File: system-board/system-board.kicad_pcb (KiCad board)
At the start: 2 copper layers, 23.9 x 79.6 mm, 15 parts, among them J1 Micro_SD_Card_Det2, J2 Conn_01x02_Socket, J3 Conn_01x02_Socket, J4 BTN_SOCKET, J5 QWIIC, Q1 IRLB8721, U1 MAX98357AETE+T

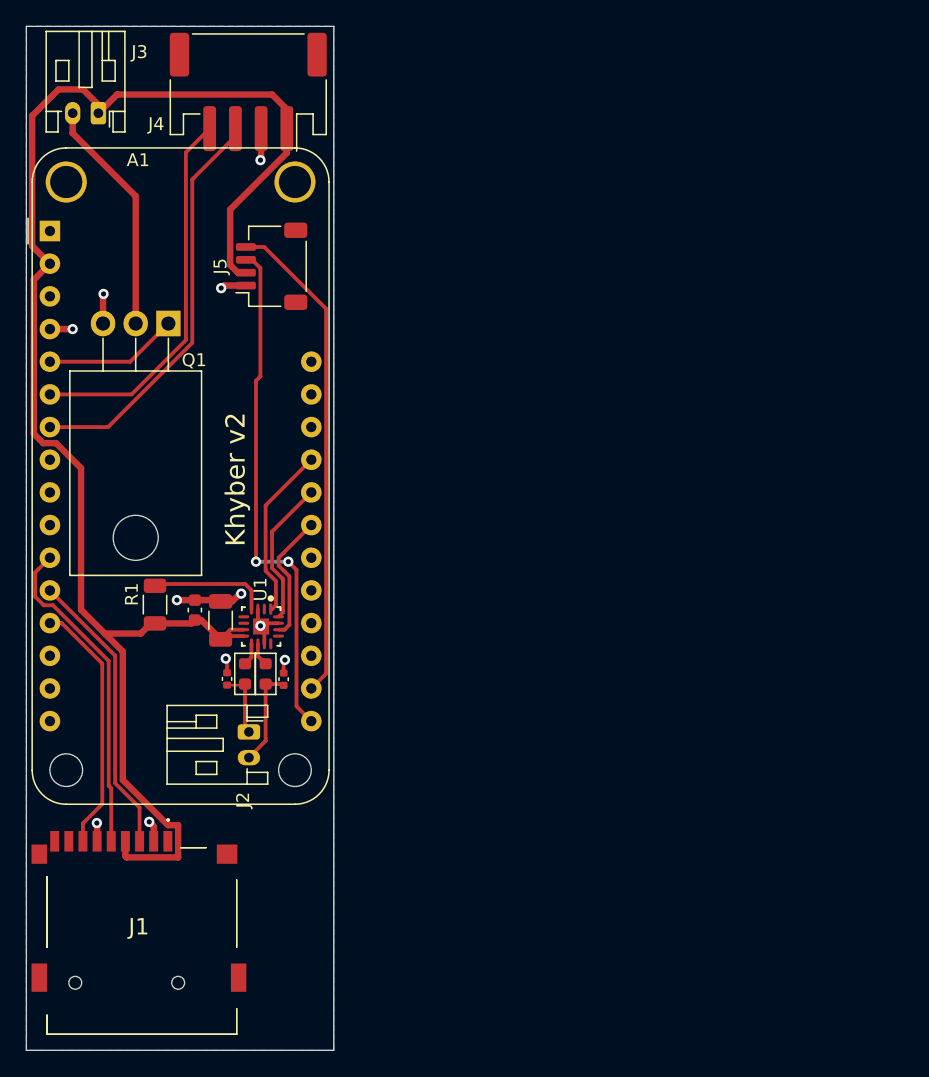
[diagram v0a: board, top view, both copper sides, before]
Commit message: Do some calculations, overhaul system-board to be a single board, not a Feather add-on.
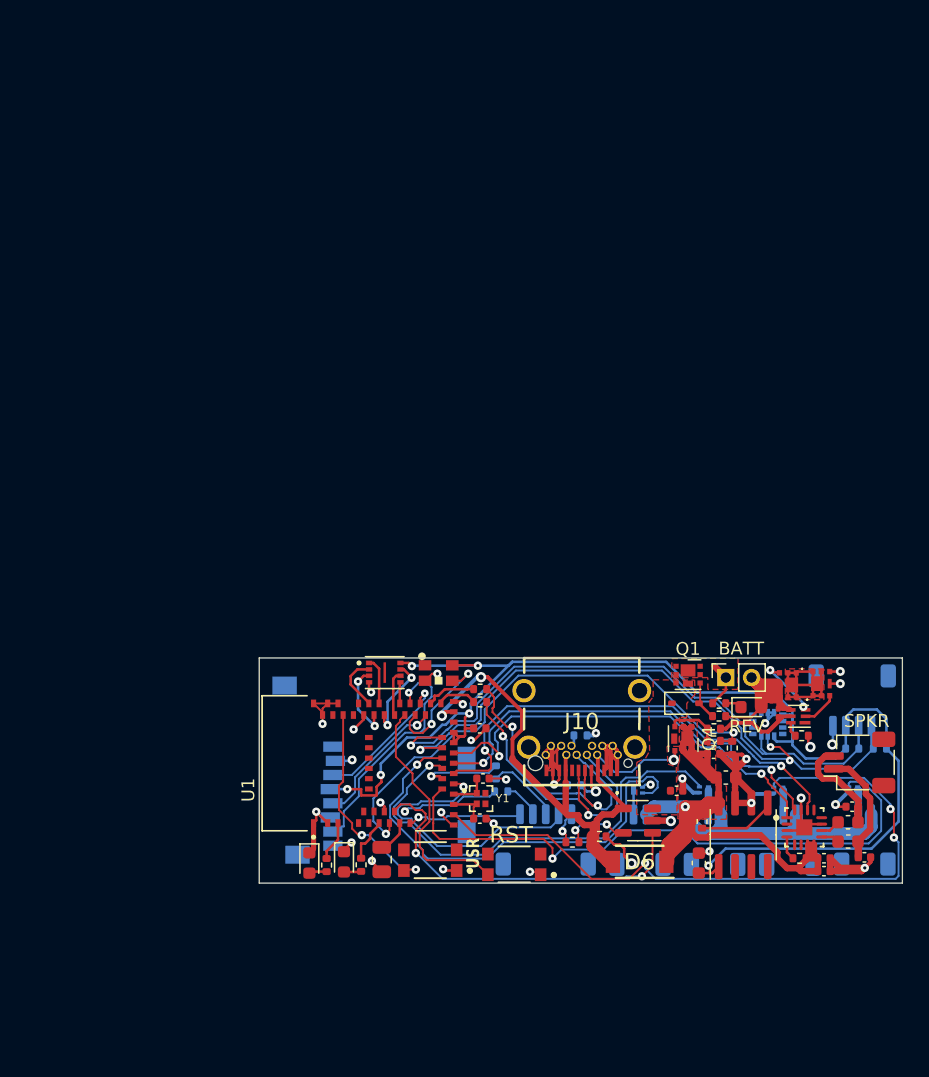
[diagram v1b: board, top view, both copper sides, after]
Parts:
- removed A1: Adafruit_Feather_Generic, Module:Adafruit_Feather_WithMountingHoles
- added C10: 0.1 uF, Capacitor_SMD:C_0201_0603Metric, F.Cu at (110.8, 95.4)
- added C11: 4.7u, Capacitor_SMD:C_0603_1608Metric, F.Cu at (106.7, 100.4)
- added C12: 4.7u, Capacitor_SMD:C_0603_1608Metric, F.Cu at (104.6, 107.0)
- added C15: 10u, Capacitor_SMD:C_0402_1005Metric, F.Cu at (105.7, 98.5)
- added C5: 220p, Capacitor_SMD:C_0402_1005Metric, F.Cu at (116.5, 102.7)
- added C6: 220p, Capacitor_SMD:C_0402_1005Metric, F.Cu at (117.5, 106.6)
- added C7: 10u, Capacitor_SMD:C_0402_1005Metric, F.Cu at (114.3, 106.7)
- added C8: 100 nF, Capacitor_SMD:C_0402_1005Metric, F.Cu at (114.3, 107.7)
- added C9: 10u, Capacitor_SMD:C_0402_1005Metric, F.Cu at (102.8, 101.4)
- added D1: WS2812B, Imports:WS2812B-2020, F.Cu at (84.3, 92.3)
- added D2: BLUE, LED_SMD:LED_0603_1608Metric, F.Cu at (74.3, 107.0)
- added D3: RED, LED_SMD:LED_0603_1608Metric, F.Cu at (77.0, 106.9)
- added D4: BZX38450, Diode_SMD:D_SOD-323, F.Cu at (103.5, 94.6)
- added D5: REV, LED_SMD:LED_0603_1608Metric, F.Cu at (108.6, 94.9)
- added D6: RSX501LAM20TR, Imports:SODFL4725X105N, F.Cu at (100.0, 106.9)
- added IC1: Flash_16Mb, Imports:USON-8-03x02mm-PSON50P200X300X50-9N, F.Cu at (80.2, 92.2)
- added IC2: LSM6DSLTR, Imports:LSM6DSLTR, B.Cu at (109.9, 96.3)
- added IC3: AP2115M-3.3TRG1, Package_SO:SOIC-8_3.9x4.9mm_P1.27mm, F.Cu at (108.0, 104.8)
- added J10: 217183-0001, Imports:Molex USB-C Horizontal 2171830001, F.Cu at (95.5, 96.0)
- added J6: BLADE_2, Connector_JST:JST_SH_SM02B-SRSS-TB_1x02-1MP_P1.00mm_Horizontal, B.Cu at (111.7, 105.3)
- added J7: BLADE_3, Connector_JST:JST_SH_SM02B-SRSS-TB_1x02-1MP_P1.00mm_Horizontal, B.Cu at (105.8, 105.3)
- added J8: BLADE_4, Connector_JST:JST_SH_SM02B-SRSS-TB_1x02-1MP_P1.00mm_Horizontal, B.Cu at (100.0, 105.3)
- added J9: BTNS, Connector_JST:JST_SH_SM05B-SRSS-TB_1x05-1MP_P1.00mm_Horizontal, B.Cu at (92.7, 105.2)
- added Q2: SSM6K504NU.LF, Imports:SSM6K504NULF, F.Cu at (114.1, 93.1)
- added Q3: SSM6K504NU.LF, Imports:SSM6K504NULF, F.Cu at (111.5, 93.2)
- added Q4: DMP1012UFDF, Imports:DMP1012UFDF, F.Cu at (103.4, 97.4)
- added Q5: PMZB290UNE2YL, Package_DFN_QFN:Diodes_DFN1006-3, B.Cu at (116.6, 101.3)
- added Q6: PMZB290UNE2YL, Package_DFN_QFN:Diodes_DFN1006-3, B.Cu at (110.8, 101.4)
- added Q7: PMZB290UNE2YL, Package_DFN_QFN:Diodes_DFN1006-3, B.Cu at (105.0, 101.3)
- added Q8: PMZB290UNE2YL, Package_DFN_QFN:Diodes_DFN1006-3, B.Cu at (99.8, 101.4)
- added R10: 1k, Resistor_SMD:R_0402_1005Metric, F.Cu at (106.2, 94.6)
- added R11: 2.0k, Resistor_SMD:R_0402_1005Metric, F.Cu at (94.8, 105.4)
- added R12: 200, Resistor_SMD:R_0402_1005Metric, F.Cu at (106.2, 95.6)
- added R13: 100k, Resistor_SMD:R_0402_1005Metric, F.Cu at (105.7, 97.5)
- added R14: 100k, Resistor_SMD:R_0402_1005Metric, F.Cu at (107.2, 98.1)
- added R15: 100k, Resistor_SMD:R_0402_1005Metric, F.Cu at (104.8, 103.8)
- added R16: 100k, Resistor_SMD:R_0402_1005Metric, F.Cu at (96.8, 105.0)
- added R2: 22, Resistor_SMD:R_0402_1005Metric, F.Cu at (87.6, 93.5)
- added R21: 1k, Resistor_SMD:R_0402_1005Metric, B.Cu at (88.8, 100.0)
- added R22: 1k, Resistor_SMD:R_0402_1005Metric, B.Cu at (89.2, 101.5)
- added R23: 5k1, Resistor_SMD:R_0402_1005Metric, B.Cu at (95.4, 97.1)
- added R24: 5k1, Resistor_SMD:R_0402_1005Metric, B.Cu at (94.9, 101.0)
- added R3: 1k, Resistor_SMD:R_0402_1005Metric, F.Cu at (75.6, 107.2)
- added R4: 1k, Resistor_SMD:R_0402_1005Metric, F.Cu at (78.3, 107.2)
- added R5: 2.0k, Resistor_SMD:R_0402_1005Metric, B.Cu at (116.5, 98.1)
- added R6: 2.0k, Resistor_SMD:R_0402_1005Metric, B.Cu at (118.7, 98.1)
- added R7: 1M, Resistor_SMD:R_0402_1005Metric, F.Cu at (112.4, 106.7)
- added R8: 330, Resistor_SMD:R_0402_1005Metric, F.Cu at (105.8, 96.6)
- added R9: 2.2k, Resistor_SMD:R_0402_1005Metric, F.Cu at (112.6, 97.1)
- added SW1: RST, Imports:CK_Components-KMR231NG_LFS-MFG, F.Cu at (90.2, 107.1)
- added SW2: USR, Imports:CK_Components-KMR231NG_LFS-MFG, F.Cu at (83.7, 106.8)
- added U2: MAX98357AETE+T, MaximCustom:Maxim_Integrated-T1633-4-0-V-IPC_C, F.Cu at (112.8, 104.3)
- added U3: BQ29705DSER, Package_SON:WSON-6_1.5x1.5mm_P0.5mm, F.Cu at (112.3, 95.6)
- added U4: MCP73832-2-OT, Package_TO_SOT_SMD:SOT-23-5, F.Cu at (99.8, 103.7)
- added Y1: 32.768k, Imports:XTAL_ECS-.327-12.5-1210B-N-TR, F.Cu at (87.7, 102.0)
- C1: footprint Capacitor_SMD:C_1206_3216Metric -> Capacitor_SMD:C_0402_1005Metric
- C2: value 0.1u -> 22p; footprint Capacitor_SMD:C_0603_1608Metric -> Capacitor_SMD:C_0402_1005Metric
- C3: value 220p -> 22p
- C4: value 220p -> 0.1 uF; footprint Capacitor_SMD:C_0402_1005Metric -> Capacitor_SMD:C_0805_2012Metric
- FB1, FB2: value FerriteBead_Small -> FB_Sm; footprint PCM_Ferrite_SMD_AKL:Ferrite_0603_1608Metric -> Capacitor_SMD:C_0603_1608Metric
- J1: value Micro_SD_Card_Det2 -> BATT; footprint TF-115:TF115 -> Connector_PinSocket_2.00mm:PinSocket_1x02_P2.00mm_Vertical
- J2: value Conn_01x02_Socket -> GTFP08431BEU; footprint Connector_JST:JST_PH_S2B-PH-K_1x02_P2.00mm_Horizontal -> Imports:GTFP08431BEU; moved to B.Cu
- J3: value Conn_01x02_Socket -> QWIIC; footprint Connector_JST:JST_PH_S2B-PH-K_1x02_P2.00mm_Horizontal -> Connector_JST:JST_SH_SM04B-SRSS-TB_1x04-1MP_P1.00mm_Horizontal; moved to B.Cu
- J4: value BTN_SOCKET -> SPKR; footprint Connector_JST:JST_PH_S4B-PH-SM4-TB_1x04-1MP_P2.00mm_Horizontal -> Connector_JST:JST_SH_SM02B-SRSS-TB_1x02-1MP_P1.00mm_Horizontal
- J5: value QWIIC -> BLADE_1; footprint Connector_JST:JST_SH_SM04B-SRSS-TB_1x04-1MP_P1.00mm_Horizontal -> Connector_JST:JST_SH_SM02B-SRSS-TB_1x02-1MP_P1.00mm_Horizontal; moved to B.Cu
- Q1: value IRLB8721 -> DMP1012UFDF; footprint Package_TO_SOT_THT:TO-220-3_Horizontal_TabDown -> Imports:DMP1012UFDF
- R1: value 1M -> 22; footprint Resistor_SMD:R_1206_3216Metric -> Resistor_SMD:R_0402_1005Metric
- U1: value MAX98357AETE+T -> MDBT50Q-1MV2; footprint MaximCustom:Maxim_Integrated-T1633-4-0-V-IPC_C -> Imports:XCVR_MDBT50Q-1MV2
- moved J3 74.3 mm to (116.5, 94.4), turned to 0 degrees
- moved J4 70.5 mm to (117.1, 99.2), turned to 90 degrees
- moved J5 64.1 mm to (117.5, 105.2), turned to 180 degrees
- moved J1 49.6 mm to (106.7, 92.6), turned to 90 degrees
- moved Q1 48.8 mm to (103.7, 92.4), turned to 0 degrees
- moved FB2 48.7 mm to (116.2, 105.4), turned to 180 degrees
- moved FB1 46.7 mm to (116.2, 103.9), turned to 180 degrees
- moved C2 27.4 mm to (87.5, 103.6), turned to 0 degrees
- moved R1 26.4 mm to (87.6, 94.5), turned to 180 degrees
- moved C1 21.8 mm to (87.5, 96.6), turned to 180 degrees
- moved C3 21.3 mm to (87.8, 100.5), turned to 0 degrees
- moved C4 16.0 mm to (79.9, 106.8), turned to 90 degrees
- moved U1 13.2 mm to (78.4, 99.3), turned to 90 degrees
- moved J2 10.3 mm to (79.5, 99.8), turned to 90 degrees
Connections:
- C2 pad 1: VCC -> /XL1
- C3 pad 1: GND -> /XL2
- C3 pad 2: /SPKR_P -> GND
- C4 pad 2: /SPKR_N -> /AREF
- FB1 pad 1: /SPKR_N -> /i2s_amp/SPKR_N
- FB1 pad 2: /SOUND_OUT_N -> /i2s_amp/SOUND_OUT_N
- FB2 pad 1: /SPKR_P -> /i2s_amp/SPKR_P
- FB2 pad 2: /SOUND_OUT_P -> /i2s_amp/SOUND_OUT_P
- J1 pad 1: unconnected-(J1-DAT2-Pad1) -> /Power Management/BATT_RAW_+
- J1 pad 2: GND -> /Power Management/BATT_RAW_-
- J2 pad 1: /SPKR_P -> unconnected-(J2-DAT2-Pad1)
- J2 pad 2: /SPKR_N -> GND
- J3 pad 1: VCC -> GND
- J3 pad 2: Net-(J3-Pin_2) -> VCC
- J4 pad 1: VCC -> /i2s_amp/SPKR_P
- J4 pad 2: GND -> /i2s_amp/SPKR_N
- J5 pad 1: GND -> VDD
- J5 pad 2: VCC -> /Blade LED Out/Blade_1_Out
- Q1 pad 1: Net-(A1-A0) -> /Power Management/BATT_RAW_+
- Q1 pad 2: Net-(J3-Pin_2) -> Net-(D4-A)
- Q1 pad 3: GND -> /Power Management/BATT_PROT_+
- R1 pad 1: Net-(U1-~{SD_MODE}) -> /CONN_USB_D-
- R1 pad 2: VCC -> /MCU_USB_D-
- U1 pad 1: /DIN -> GND
- U1 pad 10: /SOUND_OUT_N -> /VDIV
- U1 pad 11: GND -> /A4
- U1 pad 12: unconnected-(U1-NC-Pad12) -> /AREF
- U1 pad 13: unconnected-(U1-NC-Pad13) -> /A3
- U1 pad 14: /LRC -> /A2
- U1 pad 16: /BCLK -> /D10
- U1 pad 17: GND -> /XL1
- U1 pad 2: unconnected-(U1-GAIN_SLOT-Pad2) -> GND
- U1 pad 3: GND -> /LED2
- U1 pad 4: Net-(U1-~{SD_MODE}) -> unconnected-(U1-P1.11-Pad4)
- U1 pad 7: VCC -> unconnected-(U1-P1.14-Pad7)
- U1 pad 8: VCC -> /LED1
- U1 pad 9: /SOUND_OUT_P -> GND
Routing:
- net GND: track 23.4 -> 106.6 mm, vias 11 -> 34
- net VDD: track 0.00 -> 81.4 mm, vias 0 -> 1
- net /D10: track 0.00 -> 54.1 mm, vias 0 -> 3
- net /Power Management/VBUS: track 0.00 -> 51.6 mm, vias 0 -> 3
- net /SCL: track 0.00 -> 49.1 mm, vias 0 -> 3
- net /SDA: track 0.00 -> 48.1 mm, vias 0 -> 1
- net /D9: track 0.00 -> 47.4 mm, vias 0 -> 1
- net Net-(A1-SDA): track 40.6 -> 0.00 mm, vias 2 -> 0
- net /VDIV: track 0.00 -> 40.1 mm, vias 0 -> 2
- net Net-(A1-SCL): track 38.2 -> 0.00 mm
- net /D11: track 0.00 -> 36.5 mm, vias 0 -> 2
- net /D6: track 0.00 -> 36.1 mm, vias 0 -> 1
- net /D5: track 0.00 -> 35.7 mm, vias 0 -> 1
- net /D12: track 0.00 -> 34.1 mm, vias 0 -> 2
- net /D13: track 0.00 -> 33.7 mm, vias 0 -> 2
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- added copper zone on F.Cu, net /Power Management/BATT_PROT_+
- added copper zone on F.Cu, net /Power Management/BATT_RAW_+
- added copper zone on In1.Cu, net GND
- added copper zone on In2.Cu, net GND
- added copper zone on F.Cu, net Net-(Q2-D)
- added copper zone on F.Cu, net VDD
- removed copper zone on B.Cu, net GND
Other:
- board size 23.9 x 79.6 mm -> 50 x 17.5 mm
- copper layers 2 -> 4
- board text removed: "Khyber v2"

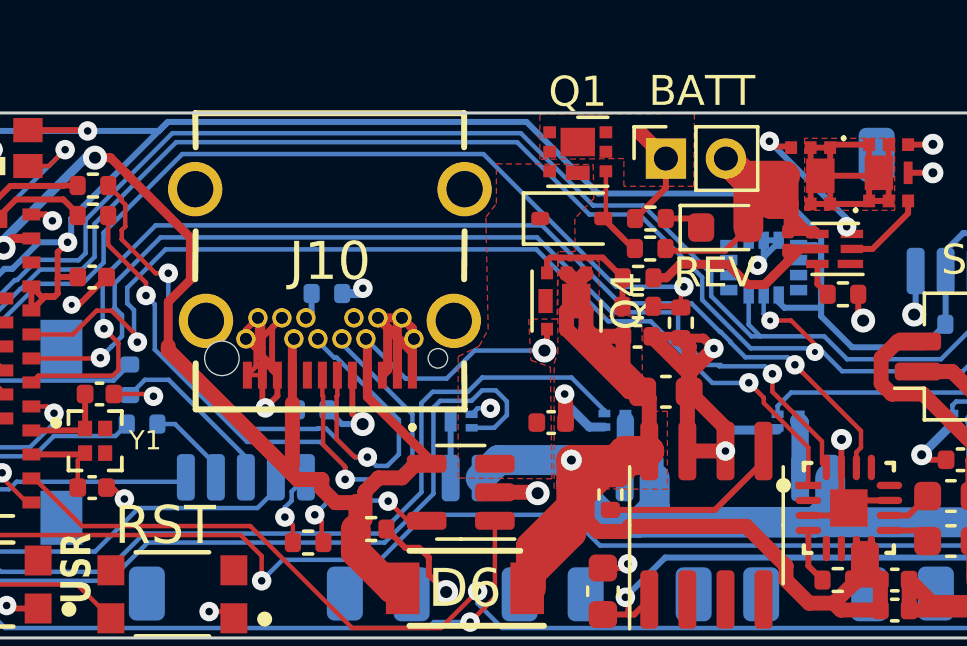
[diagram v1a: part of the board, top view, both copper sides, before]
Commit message: Add most of the missing 3D models, some tweaks
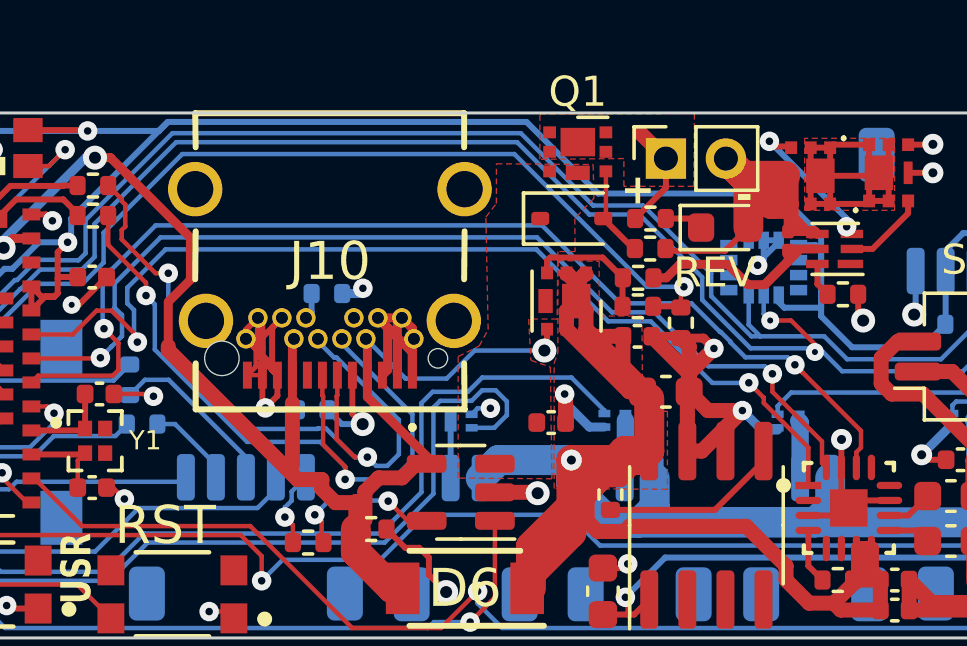
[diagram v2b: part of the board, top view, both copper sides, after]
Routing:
- net GND: track 106.6 -> 107.9 mm
- net /D12: track 34.1 -> 33.5 mm
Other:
- board text added: "+"
- board text added: "-"

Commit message: Add imported footprints & models
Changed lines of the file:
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@@
     (pad "2" smd roundrect (at 0.5 -2 90) (size 0.6 1.55) (layers "F.Cu" "F.Paste" "F.Mask") (roundrect_rratio 0.25)
       (net 4 "/i2s_amp/SPKR_N") (pinfunction "Pin_2") (pintype "passive"))
-    (pad "MP" smd roundrect (at -1.8 1.875 90) (size 1.2 1.8) (layers "F.Cu" "F.Paste" "F.Mask") (roundrect_rratio 0.208333))
-    (pad "MP" smd roundrect (at 1.8 1.875 90) (size 1.2 1.8) (layers "F.Cu" "F.Paste" "F.Mask") (roundrect_rratio 0.208333))
+    (pad "MP" smd roundrect (at -1.8 1.875 90) (size 1.2 1.8) (layers "F.Cu" "F.Paste" "F.Mask") (roundrect_rratio 0.2083333333))
+    (pad "MP" smd roundrect (at 1.8 1.875 90) (size 1.2 1.8) (layers "F.Cu" "F.Paste" "F.Mask") (roundrect_rratio 0.2083333333))
     (model "${KICAD6_3DMODEL_DIR}/Connector_JST.3dshapes/JST_SH_SM02B-SRSS-TB_1x02-1MP_P1.00mm_Horizontal.wrl"
       (offset (xyz 0 0 0))
@@
     (pad "5" smd roundrect (at 2 2 180) (size 0.6 1.55) (layers "B.Cu" "B.Paste" "B.Mask") (roundrect_rratio 0.25)
       (net 44 "/A2") (pinfunction "Pin_5") (pintype "passive"))
-    (pad "MP" smd roundrect (at -3.3 -1.875 180) (size 1.2 1.8) (layers "B.Cu" "B.Paste" "B.Mask") (roundrect_rratio 0.208333))
-    (pad "MP" smd roundrect (at 3.3 -1.875 180) (size 1.2 1.8) (layers "B.Cu" "B.Paste" "B.Mask") (roundrect_rratio 0.208333))
+    (pad "MP" smd roundrect (at -3.3 -1.875 180) (size 1.2 1.8) (layers "B.Cu" "B.Paste" "B.Mask") (roundrect_rratio 0.2083333333))
+    (pad "MP" smd roundrect (at 3.3 -1.875 180) (size 1.2 1.8) (layers "B.Cu" "B.Paste" "B.Mask") (roundrect_rratio 0.2083333333))
     (model "${KICAD6_3DMODEL_DIR}/Connector_JST.3dshapes/JST_SH_SM05B-SRSS-TB_1x05-1MP_P1.00mm_Horizontal.wrl"
       (offset (xyz 0 0 0))
@@
     (pad "4" smd roundrect (at 1.5 2) (size 0.6 1.55) (layers "B.Cu" "B.Paste" "B.Mask") (roundrect_rratio 0.25)
       (net 42 "/SCL") (pinfunction "Pin_4") (pintype "passive"))
-    (pad "MP" smd roundrect (at -2.8 -1.875) (size 1.2 1.8) (layers "B.Cu" "B.Paste" "B.Mask") (roundrect_rratio 0.208333))
-    (pad "MP" smd roundrect (at 2.8 -1.875) (size 1.2 1.8) (layers "B.Cu" "B.Paste" "B.Mask") (roundrect_rratio 0.208333))
+    (pad "MP" smd roundrect (at -2.8 -1.875) (size 1.2 1.8) (layers "B.Cu" "B.Paste" "B.Mask") (roundrect_rratio 0.2083333333))
+    (pad "MP" smd roundrect (at 2.8 -1.875) (size 1.2 1.8) (layers "B.Cu" "B.Paste" "B.Mask") (roundrect_rratio 0.2083333333))
     (model "${KICAD6_3DMODEL_DIR}/Connector_JST.3dshapes/JST_SH_SM04B-SRSS-TB_1x04-1MP_P1.00mm_Horizontal.wrl"
       (offset (xyz 0 0 0))
@@
     (pad "2" smd roundrect (at 0.5 2 180) (size 0.6 1.55) (layers "B.Cu" "B.Paste" "B.Mask") (roundrect_rratio 0.25)
       (net 94 "/Blade LED Out/Blade_4_Out") (pinfunction "Pin_2") (pintype "passive"))
-    (pad "MP" smd roundrect (at -1.8 -1.875 180) (size 1.2 1.8) (layers "B.Cu" "B.Paste" "B.Mask") (roundrect_rratio 0.208333))
-    (pad "MP" smd roundrect (at 1.8 -1.875 180) (size 1.2 1.8) (layers "B.Cu" "B.Paste" "B.Mask") (roundrect_rratio 0.208333))
+    (pad "MP" smd roundrect (at -1.8 -1.875 180) (size 1.2 1.8) (layers "B.Cu" "B.Paste" "B.Mask") (roundrect_rratio 0.2083333333))
+    (pad "MP" smd roundrect (at 1.8 -1.875 180) (size 1.2 1.8) (layers "B.Cu" "B.Paste" "B.Mask") (roundrect_rratio 0.2083333333))
     (model "${KICAD6_3DMODEL_DIR}/Connector_JST.3dshapes/JST_SH_SM02B-SRSS-TB_1x02-1MP_P1.00mm_Horizontal.wrl"
       (offset (xyz 0 0 0))
@@
     (pad "2" smd roundrect (at 0.5 2 180) (size 0.6 1.55) (layers "B.Cu" "B.Paste" "B.Mask") (roundrect_rratio 0.25)
       (net 93 "/Blade LED Out/Blade_3_Out") (pinfunction "Pin_2") (pintype "passive"))
-    (pad "MP" smd roundrect (at -1.8 -1.875 180) (size 1.2 1.8) (layers "B.Cu" "B.Paste" "B.Mask") (roundrect_rratio 0.208333))
-    (pad "MP" smd roundrect (at 1.8 -1.875 180) (size 1.2 1.8) (layers "B.Cu" "B.Paste" "B.Mask") (roundrect_rratio 0.208333))
+    (pad "MP" smd roundrect (at -1.8 -1.875 180) (size 1.2 1.8) (layers "B.Cu" "B.Paste" "B.Mask") (roundrect_rratio 0.2083333333))
+    (pad "MP" smd roundrect (at 1.8 -1.875 180) (size 1.2 1.8) (layers "B.Cu" "B.Paste" "B.Mask") (roundrect_rratio 0.2083333333))
     (model "${KICAD6_3DMODEL_DIR}/Connector_JST.3dshapes/JST_SH_SM02B-SRSS-TB_1x02-1MP_P1.00mm_Horizontal.wrl"
       (offset (xyz 0 0 0))
@@
     (pad "2" smd roundrect (at 0.5 2 180) (size 0.6 1.55) (layers "B.Cu" "B.Paste" "B.Mask") (roundrect_rratio 0.25)
       (net 91 "/Blade LED Out/Blade_1_Out") (pinfunction "Pin_2") (pintype "passive"))
-    (pad "MP" smd roundrect (at -1.8 -1.875 180) (size 1.2 1.8) (layers "B.Cu" "B.Paste" "B.Mask") (roundrect_rratio 0.208333))
-    (pad "MP" smd roundrect (at 1.8 -1.875 180) (size 1.2 1.8) (layers "B.Cu" "B.Paste" "B.Mask") (roundrect_rratio 0.208333))
+    (pad "MP" smd roundrect (at -1.8 -1.875 180) (size 1.2 1.8) (layers "B.Cu" "B.Paste" "B.Mask") (roundrect_rratio 0.2083333333))
+    (pad "MP" smd roundrect (at 1.8 -1.875 180) (size 1.2 1.8) (layers "B.Cu" "B.Paste" "B.Mask") (roundrect_rratio 0.2083333333))
     (model "${KICAD6_3DMODEL_DIR}/Connector_JST.3dshapes/JST_SH_SM02B-SRSS-TB_1x02-1MP_P1.00mm_Horizontal.wrl"
       (offset (xyz 0 0 0))
@@
     (pad "2" smd roundrect (at 0.5 2 180) (size 0.6 1.55) (layers "B.Cu" "B.Paste" "B.Mask") (roundrect_rratio 0.25)
       (net 92 "/Blade LED Out/Blade_2_Out") (pinfunction "Pin_2") (pintype "passive"))
-    (pad "MP" smd roundrect (at -1.8 -1.875 180) (size 1.2 1.8) (layers "B.Cu" "B.Paste" "B.Mask") (roundrect_rratio 0.208333))
-    (pad "MP" smd roundrect (at 1.8 -1.875 180) (size 1.2 1.8) (layers "B.Cu" "B.Paste" "B.Mask") (roundrect_rratio 0.208333))
+    (pad "MP" smd roundrect (at -1.8 -1.875 180) (size 1.2 1.8) (layers "B.Cu" "B.Paste" "B.Mask") (roundrect_rratio 0.2083333333))
+    (pad "MP" smd roundrect (at 1.8 -1.875 180) (size 1.2 1.8) (layers "B.Cu" "B.Paste" "B.Mask") (roundrect_rratio 0.2083333333))
     (model "${KICAD6_3DMODEL_DIR}/Connector_JST.3dshapes/JST_SH_SM02B-SRSS-TB_1x02-1MP_P1.00mm_Horizontal.wrl"
       (offset (xyz 0 0 0))
